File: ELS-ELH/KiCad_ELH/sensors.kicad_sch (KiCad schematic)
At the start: 23 parts, among them J10 COM CTR-MAIN, J2 MOSFETS MAIN, J4 Pressure Transducer, J7 Sensors

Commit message: Components preliminar distribution
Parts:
- removed J10: COM CTR-MAIN, ELH_Library:2Pin Header, symbol Connector:Conn_01x02_Socket
- removed J2: MOSFETS MAIN, ELH_Library:2Pin Header, symbol Connector:Conn_01x02_Socket
- removed J4: Pressure Transducer, ELH_Library:3Pin Header, symbol Connector:Conn_01x03_Socket
- removed J7: Sensors, ELH_Library:2Pin Header, symbol Connector:Conn_01x02_Socket
- added J11: Conn_01x09_Socket, Connector_Hirose:Hirose_DF13-09P-1.25DSA_1x09_P1.25mm_Vertical, symbol Connector:Conn_01x09_Socket
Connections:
- net +3.3V: now also J11.5 (Pin_5)
- net +5VA: now also J11.7 (Pin_7)
- net GND1: now also J11.6 (Pin_6), J11.8 (Pin_8)
- net MOS1_2: now also J11.1 (Pin_1)
- net MOS2_2: now also J11.2 (Pin_2)
- net PT_ADC2: now also J11.9 (Pin_9)
- net UART1_RX_2: now also J11.4 (Pin_4)
- net UART1_TX_2: now also J11.3 (Pin_3)
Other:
- note added: "Headers"
- note removed: "Screw Terminals"

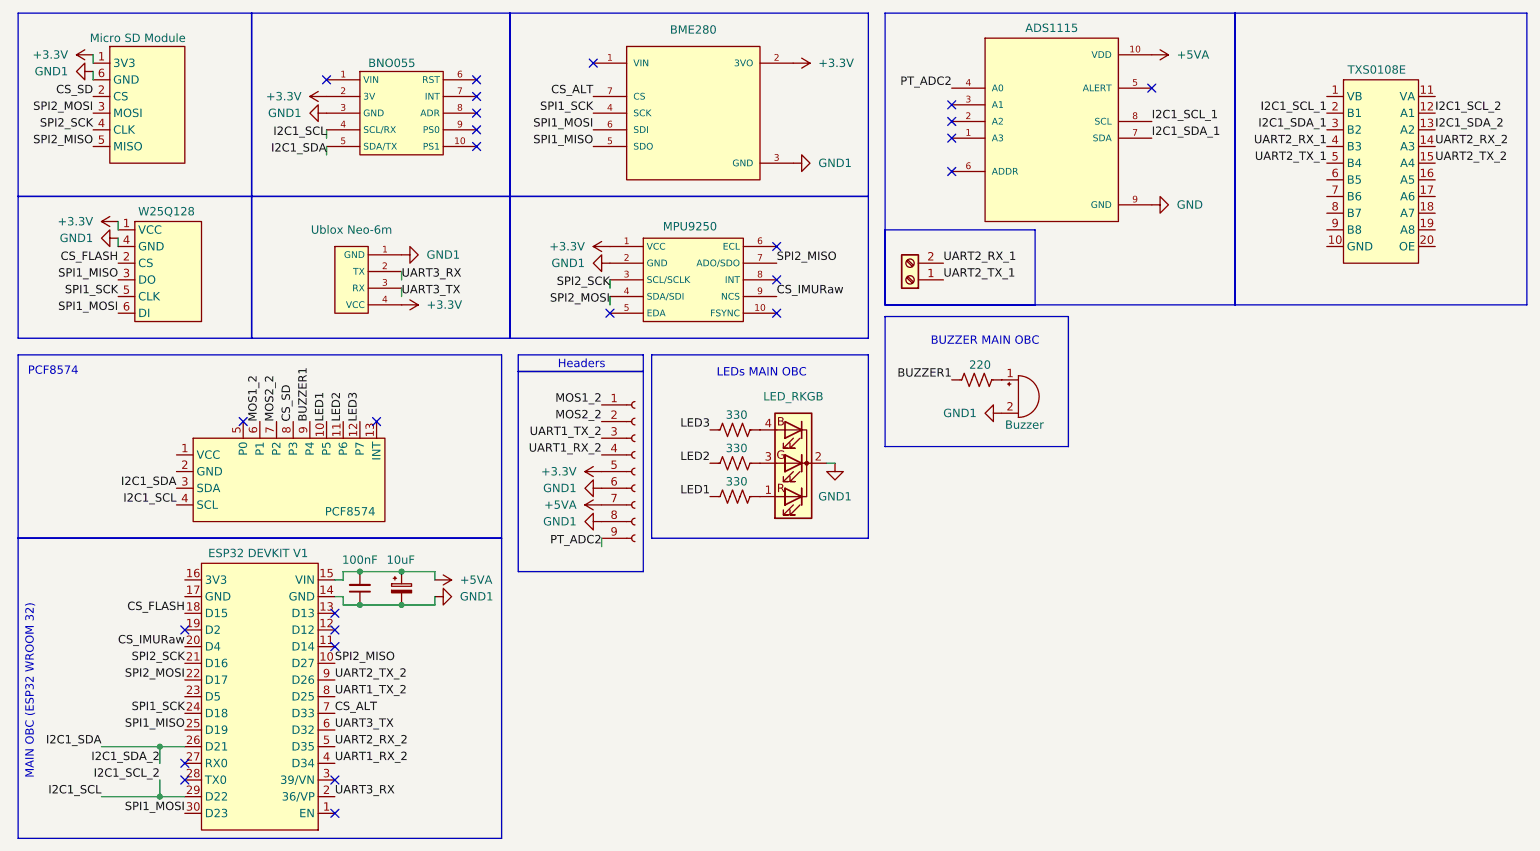
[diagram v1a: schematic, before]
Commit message: Editing some footprints and connections
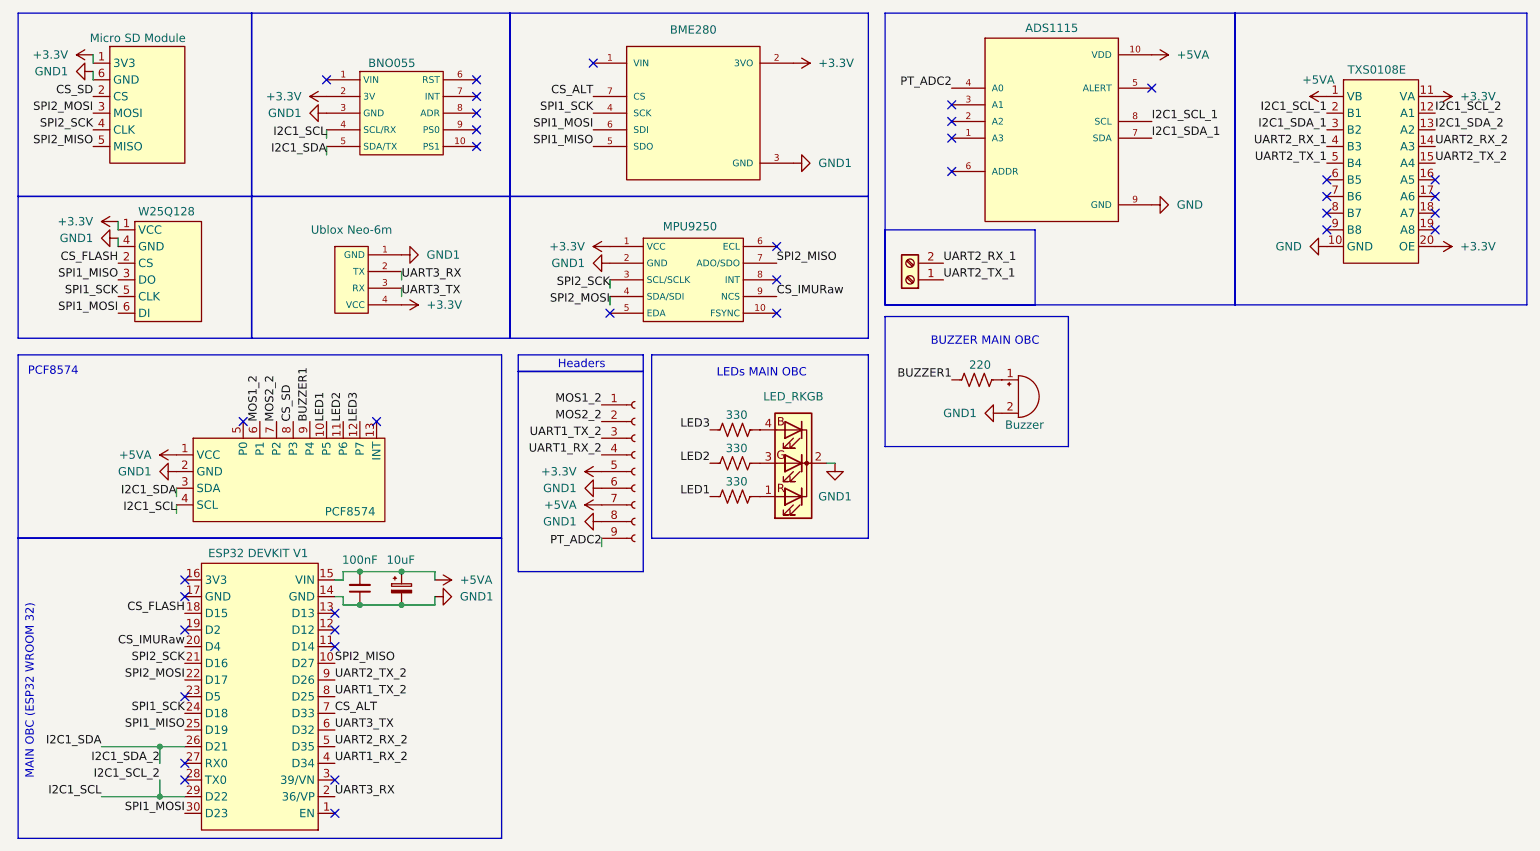
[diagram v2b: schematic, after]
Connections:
- net +3.3V: now also Converter1.11 (VA), Converter1.20 (OE)
- net +5VA: now also Adapter1.1 (VCC), Converter1.1 (VB)
- net GND: now also Converter1.10 (GND)
- net GND1: now also Adapter1.2 (GND)
- no-connect marks 26 -> 37
